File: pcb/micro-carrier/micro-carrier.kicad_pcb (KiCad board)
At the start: 2 copper layers, 40.6 x 61 mm, 18 parts, among them J1 Conn_01x17, J2 Conn_01x17, U1 P4V-MINI, U10 P4V-MINI, U11 P4V-MINI, U12 P4V-MINI, U2 P4V-MINI, U3 P4V-MINI, U4 P4V-MINI, U5 P4V-MINI, U6 P4V-MINI, U7 P4V-MINI, U8 P4V-MINI, U9 P4V-MINI

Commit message: Update proper pinout
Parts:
- moved J1 40.6 mm to (142.2, 116.8), turned to 180 degrees
- moved U12 38.1 mm to (153.7, 77.5)
- moved U7 38.1 mm to (153.7, 115.6)
- moved U8 22.9 mm to (153.7, 108.0)
- moved U11 22.9 mm to (153.7, 85.1)
- moved U9 7.62 mm to (153.7, 100.3)
- moved U10 7.62 mm to (153.7, 92.7)
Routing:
- net GND: track 154.4 -> 157.5 mm
- net +5V: track 114.6 -> 115.7 mm
- net /OUT12: track 11.0 -> 10.5 mm
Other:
- board text added: "USB"

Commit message: Update version name silkmask
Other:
- board text added: "Micro Carrier V1.1"
- board text removed: "Micro Carrier V1"
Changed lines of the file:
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@@
 		)
 		(fp_text user "${REFERENCE}"
-			(at 0 20.32 270)
+			(at 0 20.32 -90)
 			(layer "F.Fab")
 			(effects
@@
 		(layer "Edge.Cuts")
 	)
-	(gr_text "Micro Carrier V1"
-		(at 135.89 78.74 90)
+	(gr_text "Micro Carrier V1.1"
+		(at 135.89 76.835 90)
 		(layer "B.SilkS")
 		(effects

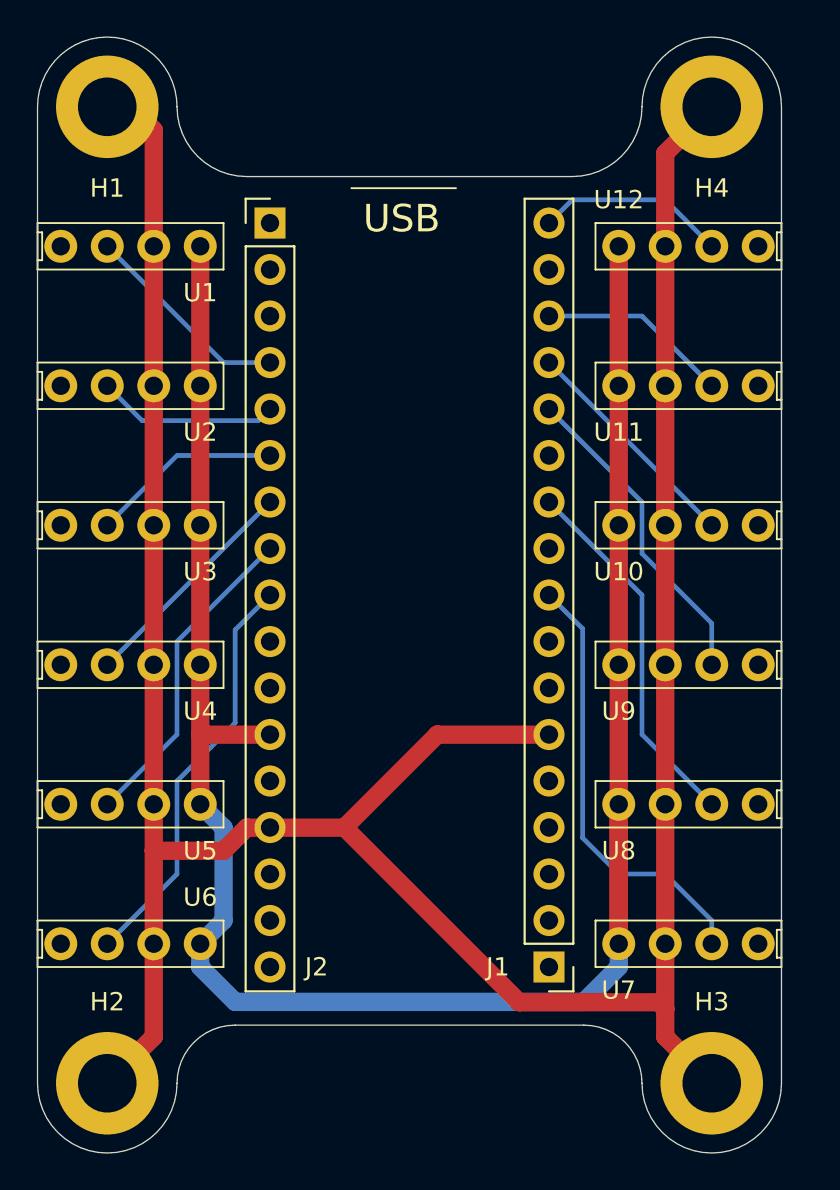
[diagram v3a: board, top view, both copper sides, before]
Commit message: Add micro analog refrence silkmask
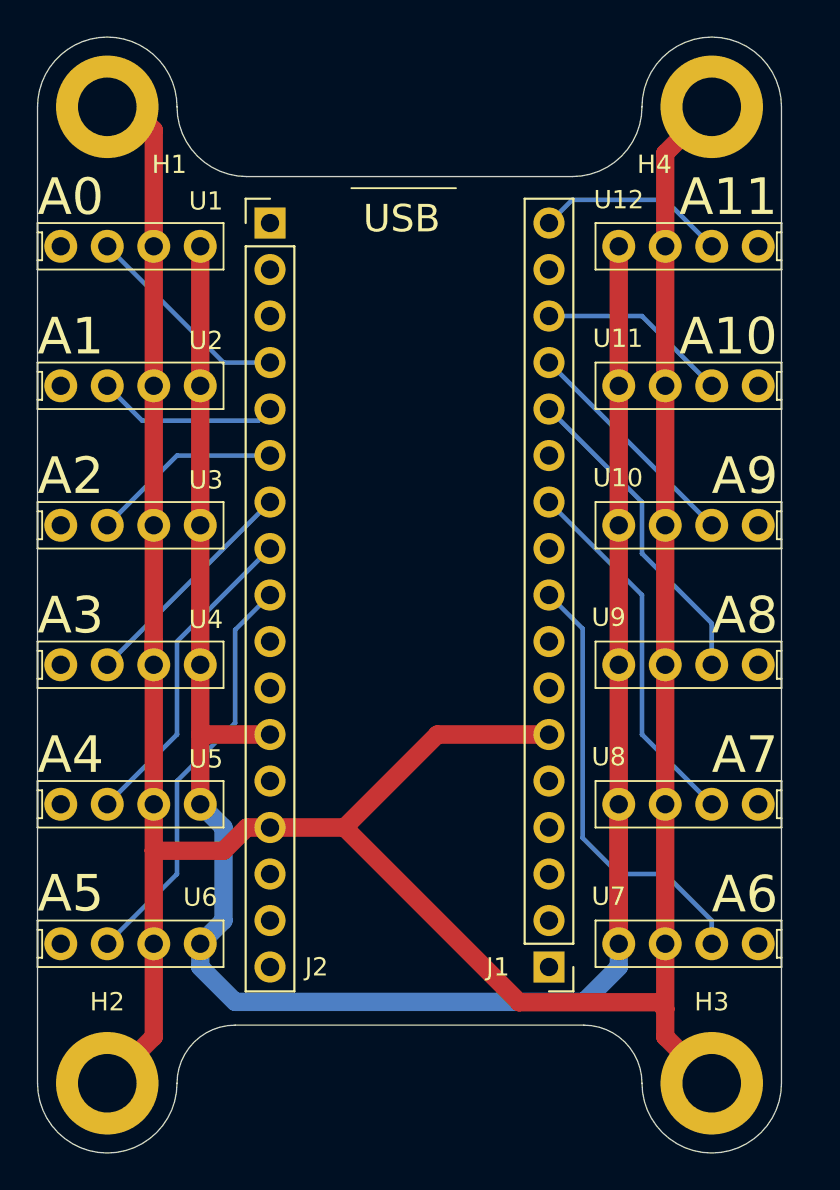
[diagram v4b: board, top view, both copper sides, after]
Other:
- board text added: "A0"
- board text added: "A1"
- board text added: "A10"
- board text added: "A11"
- board text added: "A2"
- board text added: "A3"
- board text added: "A4"
- board text added: "A5"
- board text added: "A6"
- board text added: "A7"
- board text added: "A8"
- board text added: "A9"
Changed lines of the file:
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@@
 		(at 153.67 100.33 180)
 		(property "Reference" "U9"
-			(at 7.620001 -2.54 0)
+			(at 8.17 2.59 0)
 			(unlocked yes)
 			(layer "F.SilkS")
@@
 		(at 153.67 92.71 180)
 		(property "Reference" "U10"
-			(at 7.620001 -2.54 0)
+			(at 7.67 2.59 0)
 			(unlocked yes)
 			(layer "F.SilkS")
@@
 		(at 115.57 92.71)
 		(property "Reference" "U3"
-			(at 7.62 2.54 0)
+			(at 7.93 -2.47 0)
 			(unlocked yes)
 			(layer "F.SilkS")
@@
 		(at 153.67 85.09 180)
 		(property "Reference" "U11"
-			(at 7.620001 -2.54 0)
+			(at 7.67 2.59 0)
 			(unlocked yes)
 			(layer "F.SilkS")
@@
 		(at 115.57 77.47)
 		(property "Reference" "U1"
-			(at 7.62 2.54 0)
+			(at 7.93 -2.47 0)
 			(unlocked yes)
 			(layer "F.SilkS")
@@
 		(at 153.67 115.57 180)
 		(property "Reference" "U7"
-			(at 7.62 -2.54 0)
+			(at 8.169999 2.59 0)
 			(unlocked yes)
 			(layer "F.SilkS")
@@
 		(at 115.57 100.33)
 		(property "Reference" "U4"
-			(at 7.62 2.54 0)
+			(at 7.93 -2.47 0)
 			(unlocked yes)
 			(layer "F.SilkS")
@@
 		(tags "mounting hole 3.2mm m3 din965")
 		(property "Reference" "H4"
-			(at 0 4.445 0)
+			(at -3.13 3.15 0)
 			(layer "F.SilkS")
 			(effects
@@
 		(at 115.57 107.95)
 		(property "Reference" "U5"
-			(at 7.62 2.54 0)
+			(at 7.93 -2.47 0)
 			(unlocked yes)
 			(layer "F.SilkS")
@@
 		(tags "mounting hole 3.2mm m3 din965")
 		(property "Reference" "H1"
-			(at 0 4.445 0)
+			(at 3.39 3.15 0)
 			(layer "F.SilkS")
 			(effects
@@
 		(at 153.67 107.95 180)
 		(property "Reference" "U8"
-			(at 7.620001 -2.54 0)
+			(at 8.17 2.59 0)
 			(unlocked yes)
 			(layer "F.SilkS")
@@
 		(at 115.57 85.09)
 		(property "Reference" "U2"
-			(at 7.62 2.54 0)
+			(at 7.93 -2.47 0)
 			(unlocked yes)
 			(layer "F.SilkS")
@@
 		)
 	)
+	(gr_text "A4"
+		(at 114.3 106.426 0)
+		(layer "F.SilkS")
+		(effects
+			(font
+				(size 2 2)
+				(thickness 0.3)
+			)
+			(justify left bottom)
+		)
+	)
+	(gr_text "A11"
+		(at 149.352 75.946 0)
+		(layer "F.SilkS")
+		(effects
+			(font
+				(size 2 2)
+				(thickness 0.3)
+			)
+			(justify left bottom)
+		)
+	)
+	(gr_text "A10"
+		(at 149.352 83.566 0)
+		(layer "F.SilkS")
+		(effects
+			(font
+				(size 2 2)
+				(thickness 0.3)
+			)
+			(justify left bottom)
+		)
+	)
+	(gr_text "A2"
+		(at 114.3 91.186 0)
+		(layer "F.SilkS")
+		(effects
+			(font
+				(size 2 2)
+				(thickness 0.3)
+			)
+			(justify left bottom)
+		)
+	)
 	(gr_text "USB"
 		(at 132.08 76.835 0)
@@
 			)
 			(justify left bottom)
+		)
+	)
+	(gr_text "A6"
+		(at 151.13 114.046 0)
+		(layer "F.SilkS")
+		(effects
+			(font
+				(size 2 2)
+				(thickness 0.3)
+			)
+			(justify left bottom)
+		)
+	)
+	(gr_text "A9"
+		(at 151.13 91.186 0)
+		(layer "F.SilkS")
+		(effects
+			(font
+				(size 2 2)
+				(thickness 0.3)
+			)
+			(justify left bottom)
+		)
+	)
+	(gr_text "A3"
+		(at 114.3 98.806 0)
+		(layer "F.SilkS")
+		(effects
+			(font
+				(size 2 2)
+				(thickness 0.3)
+			)
+			(justify left bottom)
+		)
+	)
+	(gr_text "A8"
+		(at 151.13 98.806 0)
+		(layer "F.SilkS")
+		(effects
+			(font
+				(size 2 2)
+				(thickness 0.3)
+			)
+			(justify left bottom)
+		)
+	)
+	(gr_text "A1"
+		(at 114.3 83.566 0)
+		(layer "F.SilkS")
+		(effects
+			(font
+				(size 2 2)
+				(thickness 0.3)
+			)
+			(justify left bottom)
+		)
+	)
+	(gr_text "A7"
+		(at 151.13 106.426 0)
+		(layer "F.SilkS")
+		(effects
+			(font
+				(size 2 2)
+				(thickness 0.3)
+			)
+			(justify left bottom)
+		)
+	)
+	(gr_text "A5"
+		(at 114.3 114 0)
+		(layer "F.SilkS")
+		(effects
+			(font
+				(size 2 2)
+				(thickness 0.3)
+			)
+			(justify left bottom)
+		)
+	)
+	(gr_text "A0"
+		(at 114.3 75.946 0)
+		(layer "F.SilkS")
+		(effects
+			(font
+				(size 2 2)
+				(thickness 0.3)
+			)
+			(justify left bottom)
